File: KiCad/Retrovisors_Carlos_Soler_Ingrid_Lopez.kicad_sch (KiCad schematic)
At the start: 22 parts, among them J1 Conn_01x02, J2 Conn_01x03, J3 Conn_01x05, J4 Conn_01x08, SW1 SW_DPST_x2, U1 PIC32MX250F128B-50I/SO, U2 DRV8906QPWPRQ1, Y1 Crystal

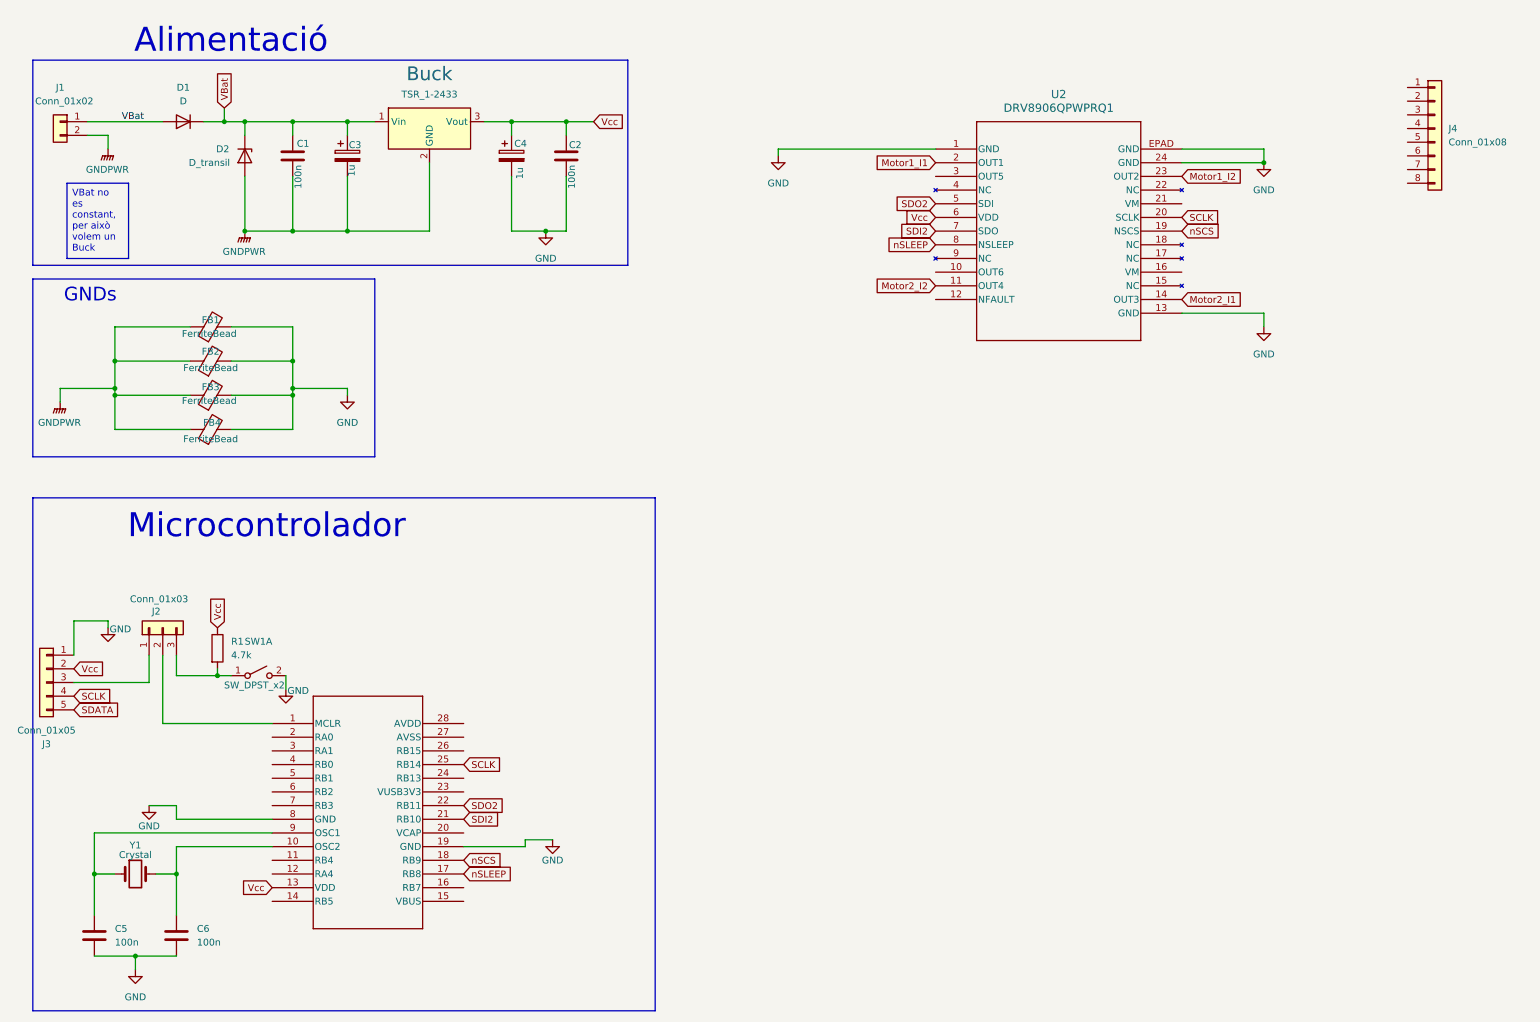
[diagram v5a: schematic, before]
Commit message: Correcio gnd, proposicio canvi de micro
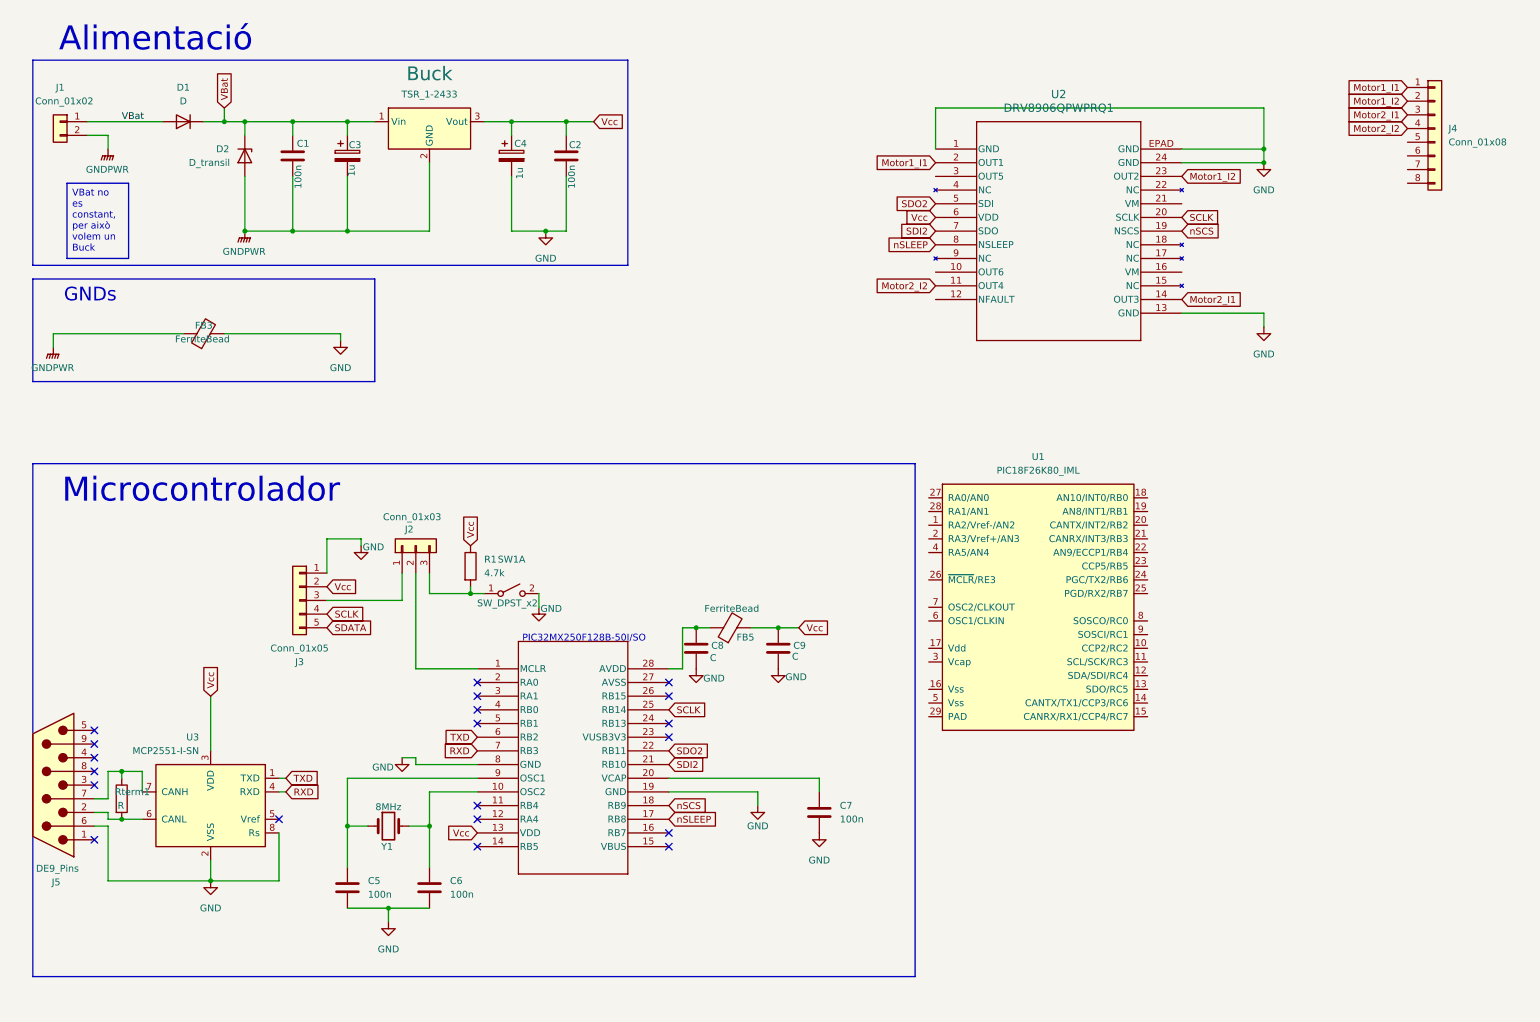
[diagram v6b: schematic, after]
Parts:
- removed FB1, FB2, FB4: FerriteBead, symbol Device:FerriteBead
- added C7: 100n, symbol Device:C
- added C8, C9: C, symbol Device:C
- added FB5: FerriteBead, symbol Device:FerriteBead
- added J5: DE9_Pins, symbol Connector:DE9_Pins
- added Rterm1: R, symbol Device:R
- added U1: PIC18F26K80_IML, Package_DFN_QFN:QFN-28-1EP_6x6mm_P0.65mm_EP4.25x4.25mm, symbol MCU_Microchip_PIC18:PIC18F26K80_IML
- added U3: MCP2551-I-SN, Package_SO:SOIC-8_3.9x4.9mm_P1.27mm, symbol Interface_CAN_LIN:MCP2551-I-SN
- PIC32MX250F128B-50I/SO: renamed from U1; footprint SOIC28-W_MC_MCH -> PIC32MX250F128B_50I_SO:SOIC28-W_MC_MCH
- Y1: value Crystal -> 8MHz
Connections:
- net GND: now also C7.2, C8.2, C9.2, J5.6, U3.2 (VSS), U3.8 (Rs)
- net Motor1_I1: now also J4.1 (Pin_1)
- net Motor1_I2: now also J4.2 (Pin_2)
- net Motor2_I1: now also J4.3 (Pin_3)
- net Motor2_I2: now also J4.4 (Pin_4)
- net Vcc: now also C9.1, FB5.2, U3.3 (VDD)
- net at PIC32MX250F128B-50I/SO.20 (VCAP): now also C7.1
- net at PIC32MX250F128B-50I/SO.28 (AVDD): now also C8.1, FB5.1
- net TXD: now reaches PIC32MX250F128B-50I/SO.6 (RB2)
- net TXD: now also U3.1 (TXD)
- net RXD: now reaches PIC32MX250F128B-50I/SO.7 (RB3)
- net RXD: now also U3.4 (RXD)
- new net: J5.2, Rterm1.2, U3.6 (CANL)
- new net: J5.7, Rterm1.1, U3.7 (CANH)
- no-connect marks 0 -> 20
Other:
- note added: "PIC32MX250F128B-50I/SO"
- moved on the sheet: C5, C6, FB3, J2, J3, R1, SW1A, Y1

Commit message: Reorganització proyecte, inici conexions CAN
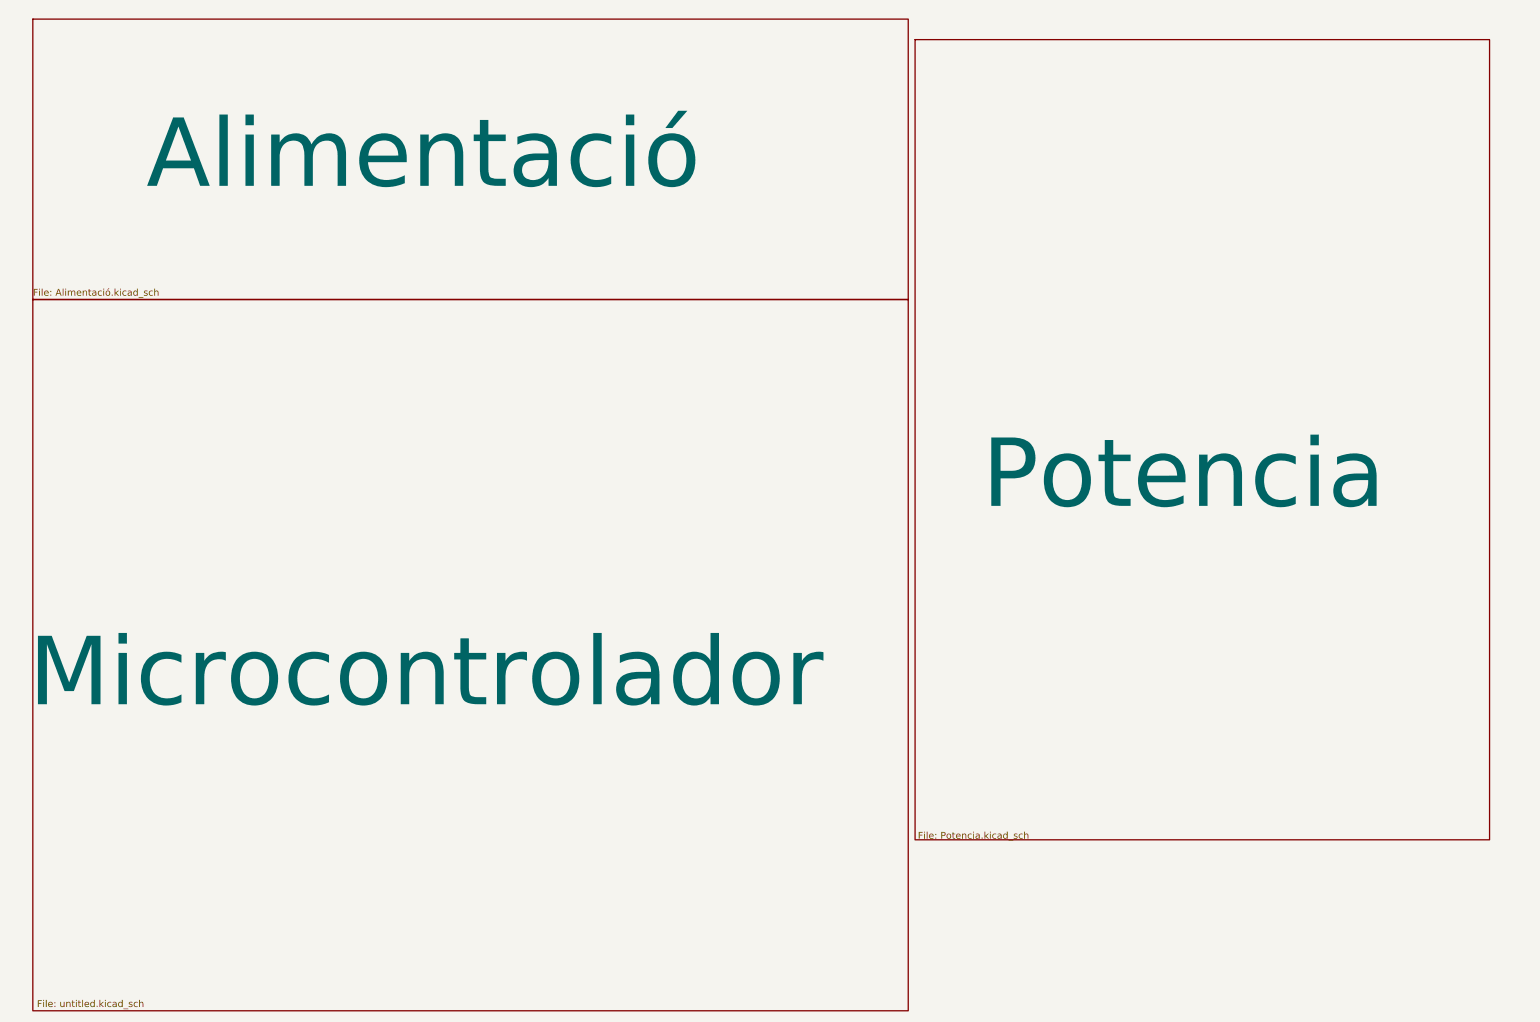
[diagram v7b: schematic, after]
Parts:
- removed Buck: TSR_1-2433, Converter_DCDC:Converter_DCDC_TRACO_TSR-1_THT, symbol Converter_DCDC:TSR_1-2433
- removed C1, C2, C5, C6, C7: 100n, symbol Device:C
- removed C3, C4: 1u, symbol Device:C_Polarized
- removed C8, C9: C, symbol Device:C
- removed D1: D, symbol Device:D
- removed D2: D_transil, symbol Device:D_Zener
- removed FB3, FB5: FerriteBead, symbol Device:FerriteBead
- removed J1: Conn_01x02, symbol Connector_Generic:Conn_01x02
- removed J2: Conn_01x03, symbol Connector_Generic:Conn_01x03
- removed J3: Conn_01x05, symbol Connector_Generic:Conn_01x05
- removed J4: Conn_01x08, symbol Connector_Generic:Conn_01x08
- removed J5: DE9_Pins, symbol Connector:DE9_Pins
- removed PIC32MX250F128B-50I/SO: PIC32MX250F128B-50I/SO, PIC32MX250F128B_50I_SO:SOIC28-W_MC_MCH, symbol PIC32MX250F128B_50I_SO:PIC32MX250F128B-50I_SO
- removed R1: 4.7k, symbol Device:R
- removed Rterm1: R, symbol Device:R
- removed SW1: SW_DPST_x2, symbol Switch:SW_DPST_x2
- removed U1: PIC18F26K80_IML, Package_DFN_QFN:QFN-28-1EP_6x6mm_P0.65mm_EP4.25x4.25mm, symbol MCU_Microchip_PIC18:PIC18F26K80_IML
- removed U2: DRV8906QPWPRQ1, HTSSOP24_PWP_TEX, symbol Drivers_motors_xy:DRV8906QPWPRQ1
- removed U3: MCP2551-I-SN, Package_SO:SOIC-8_3.9x4.9mm_P1.27mm, symbol Interface_CAN_LIN:MCP2551-I-SN
- removed Y1: 8MHz, symbol Device:Crystal
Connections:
- no-connect marks 20 -> 0
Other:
- added sheet Alimentació (Alimentació.kicad_sch)
- added sheet Microcontrolador (untitled.kicad_sch)
- added sheet Potencia (Potencia.kicad_sch)
- note removed: "Alimentació"
- note removed: "GNDs"
- note removed: "Microcontrolador"
- note removed: "PIC32MX250F128B-50I/SO"

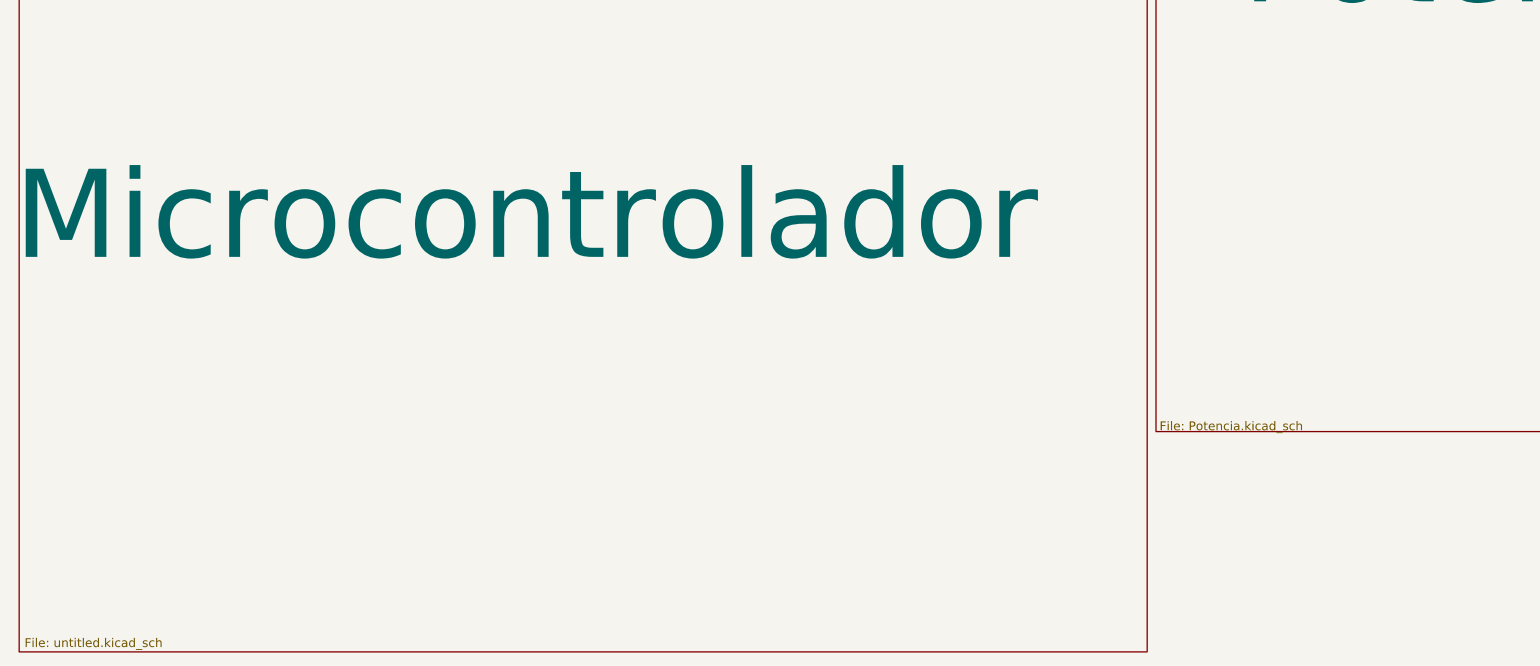
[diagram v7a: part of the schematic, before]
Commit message: Microprocessador finalissim + placement de alimentacion y micro
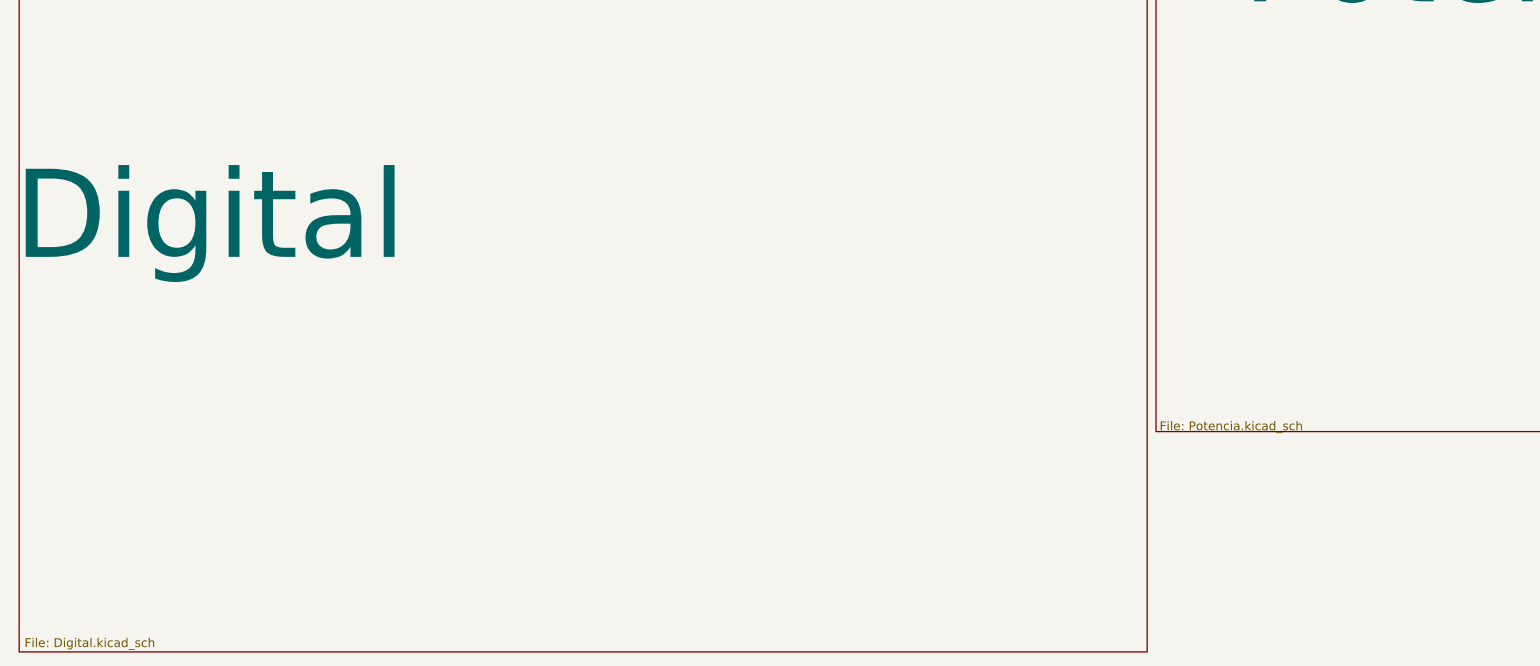
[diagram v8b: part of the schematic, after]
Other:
- sheet Microcontrolador renamed Digital
- sheet Digital: file untitled.kicad_sch -> Digital.kicad_sch
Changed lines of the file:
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@@
 			(color 0 0 0 0.0000)
 		)
-		(property "Sheetname" "Microcontrolador"
+		(property "Sheetname" "Digital"
 			(at 11.938 141.478 0)
 			(effects
@@
 			)
 		)
-		(property "Sheetfile" "untitled.kicad_sch"
+		(property "Sheetfile" "Digital.kicad_sch"
 			(at 13.462 194.818 0)
 			(effects
